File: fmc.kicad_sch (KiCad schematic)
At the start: 2 parts, among them P1 ASP-134604-01, P2 ASP-134604-01

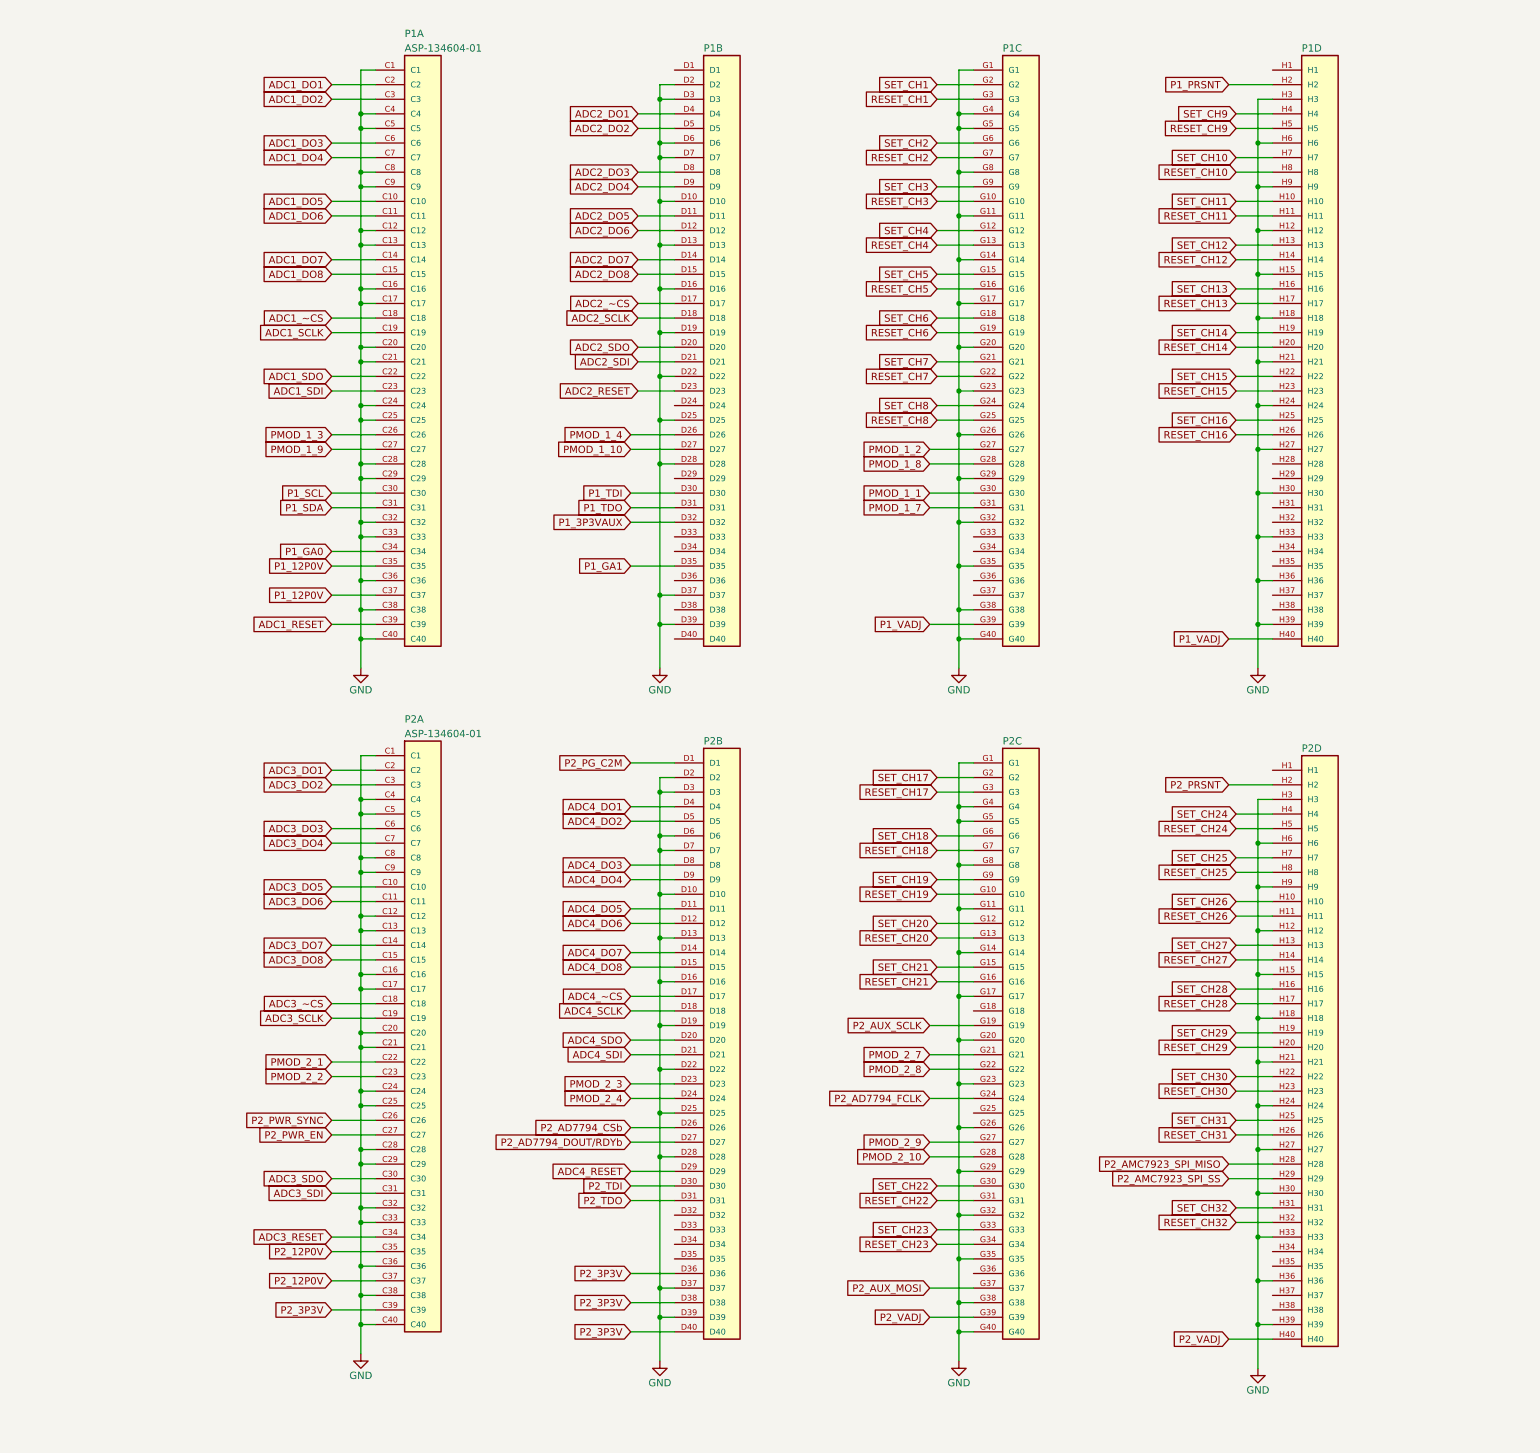
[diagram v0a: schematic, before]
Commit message: Updated Schmatics
Some outdated schematics were in the init commit. Uploded proper revision with tweaks.
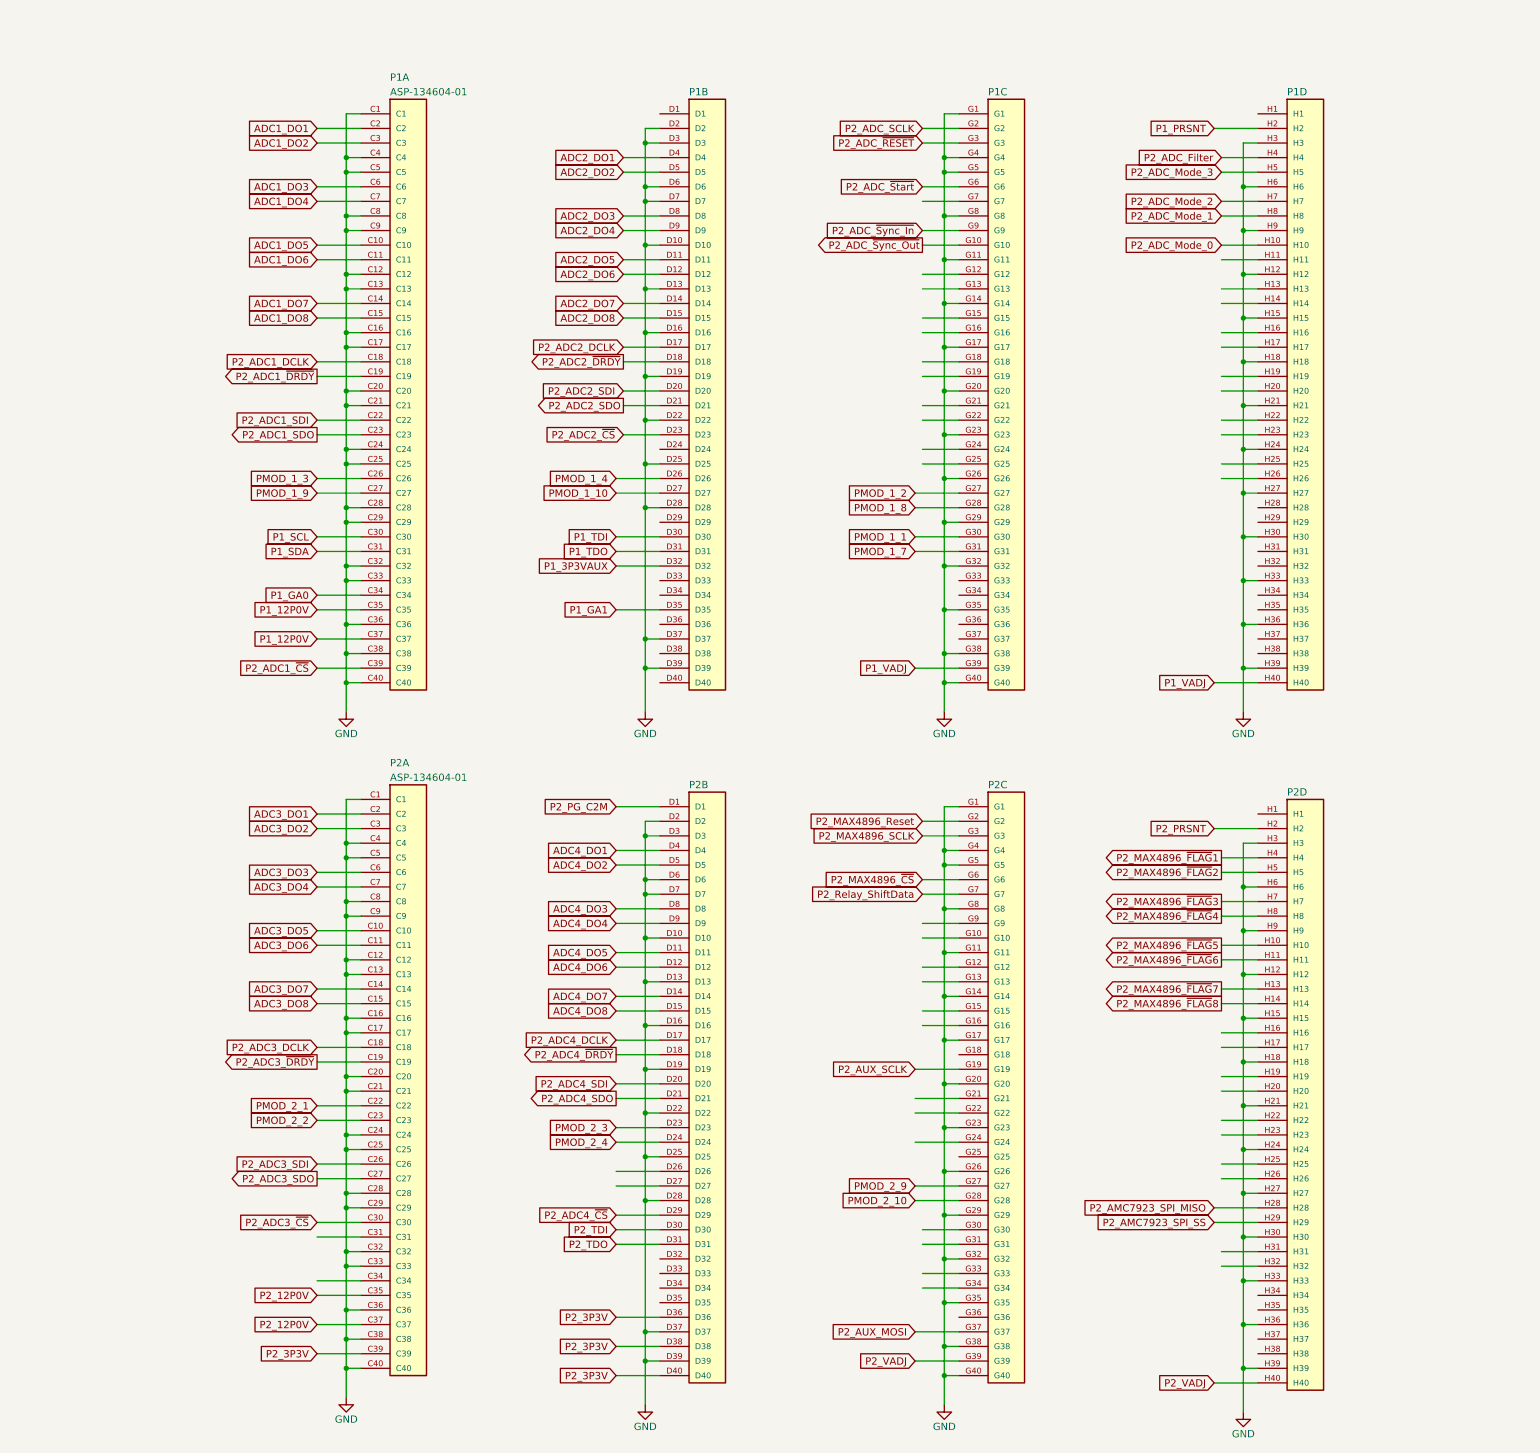
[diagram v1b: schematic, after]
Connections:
- net ADC1_RESET renamed P2_ADC1_~{CS}
- net ADC1_SCLK renamed P2_ADC1_~{DRDY}
- net ADC1_SDI renamed P2_ADC1_SDO
- net ADC1_SDO renamed P2_ADC1_SDI
- net ADC1_~CS renamed P2_ADC1_DCLK
- net ADC2_RESET renamed P2_ADC2_~{CS}
- net ADC2_SCLK renamed P2_ADC2_~{DRDY}
- net ADC2_SDI renamed P2_ADC2_SDO
- net ADC2_SDO renamed P2_ADC2_SDI
- net ADC2_~CS renamed P2_ADC2_DCLK
- net ADC3_RESET: no longer names the net of P2.C34
- net ADC3_SCLK renamed P2_ADC3_~{DRDY}
- net ADC3_SDI: no longer names the net of P2.C31
- net ADC3_SDO renamed P2_ADC3_~{CS}
- net ADC3_~CS renamed P2_ADC3_DCLK
- net ADC4_RESET renamed P2_ADC4_~{CS}
- net ADC4_SCLK renamed P2_ADC4_~{DRDY}
- net ADC4_SDI renamed P2_ADC4_SDO
- net ADC4_SDO renamed P2_ADC4_SDI
- net ADC4_~CS renamed P2_ADC4_DCLK
- net P2_AD7794_CSb: no longer names the net of P2.D26
- net P2_AD7794_DOUT/RDYb: no longer names the net of P2.D27
- net P2_AD7794_FCLK: no longer names the net of P2.G24
- net P2_PWR_EN renamed P2_ADC3_SDO
- net P2_PWR_SYNC renamed P2_ADC3_SDI
- net PMOD_2_7: no longer names the net of P2.G21
- net PMOD_2_8: no longer names the net of P2.G22
- net RESET_CH1 renamed P2_ADC_~{RESET}
- net RESET_CH10 renamed P2_ADC_Mode_1
- net RESET_CH11: no longer names the net of P1.H11
- net RESET_CH12: no longer names the net of P1.H14
- net RESET_CH13: no longer names the net of P1.H17
- net RESET_CH14: no longer names the net of P1.H20
- net RESET_CH15: no longer names the net of P1.H23
- net RESET_CH16: no longer names the net of P1.H26
- net RESET_CH17 renamed P2_MAX4896_SCLK
- net RESET_CH18 renamed P2_Relay_ShiftData
- net RESET_CH19: no longer names the net of P2.G10
- net RESET_CH2: no longer names the net of P1.G7
- net RESET_CH20: no longer names the net of P2.G13
- net RESET_CH21: no longer names the net of P2.G16
- net RESET_CH22: no longer names the net of P2.G31
- net RESET_CH23: no longer names the net of P2.G34
- net RESET_CH24 renamed P2_MAX4896_~{FLAG}2
- net RESET_CH25 renamed P2_MAX4896_~{FLAG}4
- net RESET_CH26 renamed P2_MAX4896_~{FLAG}6
- net RESET_CH27 renamed P2_MAX4896_~{FLAG}8
- net RESET_CH28: no longer names the net of P2.H17
- net RESET_CH29: no longer names the net of P2.H20
- net RESET_CH3 renamed P2_ADC_~{Sync_Out}
- net RESET_CH30: no longer names the net of P2.H23
- net RESET_CH31: no longer names the net of P2.H26
- net RESET_CH32: no longer names the net of P2.H32
- net RESET_CH4: no longer names the net of P1.G13
- net RESET_CH5: no longer names the net of P1.G16
- net RESET_CH6: no longer names the net of P1.G19
- net RESET_CH7: no longer names the net of P1.G22
- net RESET_CH8: no longer names the net of P1.G25
- net RESET_CH9 renamed P2_ADC_Mode_3
- net SET_CH1 renamed P2_ADC_SCLK
- net SET_CH10 renamed P2_ADC_Mode_2
- net SET_CH11 renamed P2_ADC_Mode_0
- net SET_CH12: no longer names the net of P1.H13
- net SET_CH13: no longer names the net of P1.H16
- net SET_CH14: no longer names the net of P1.H19
- net SET_CH15: no longer names the net of P1.H22
- net SET_CH16: no longer names the net of P1.H25
- net SET_CH17 renamed P2_MAX4896_Reset
- net SET_CH18 renamed P2_MAX4896_~{CS}
- net SET_CH19: no longer names the net of P2.G9
- net SET_CH2 renamed P2_ADC_~{Start}
- net SET_CH20: no longer names the net of P2.G12
- net SET_CH21: no longer names the net of P2.G15
- net SET_CH22: no longer names the net of P2.G30
- net SET_CH23: no longer names the net of P2.G33
- net SET_CH24 renamed P2_MAX4896_~{FLAG}1
- net SET_CH25 renamed P2_MAX4896_~{FLAG}3
- net SET_CH26 renamed P2_MAX4896_~{FLAG}5
- net SET_CH27 renamed P2_MAX4896_~{FLAG}7
- net SET_CH28: no longer names the net of P2.H16
- net SET_CH29: no longer names the net of P2.H19
- net SET_CH3 renamed P2_ADC_~{Sync_In}
- net SET_CH30: no longer names the net of P2.H22
- net SET_CH31: no longer names the net of P2.H25
- net SET_CH32: no longer names the net of P2.H31
- net SET_CH4: no longer names the net of P1.G12
- net SET_CH5: no longer names the net of P1.G15
- net SET_CH6: no longer names the net of P1.G18
- net SET_CH7: no longer names the net of P1.G21
- net SET_CH8: no longer names the net of P1.G24
- net SET_CH9 renamed P2_ADC_Filter

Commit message: Fixed FMC mapping Issue
Fixed FMC pin mapping and added FMC pin mapping excel file
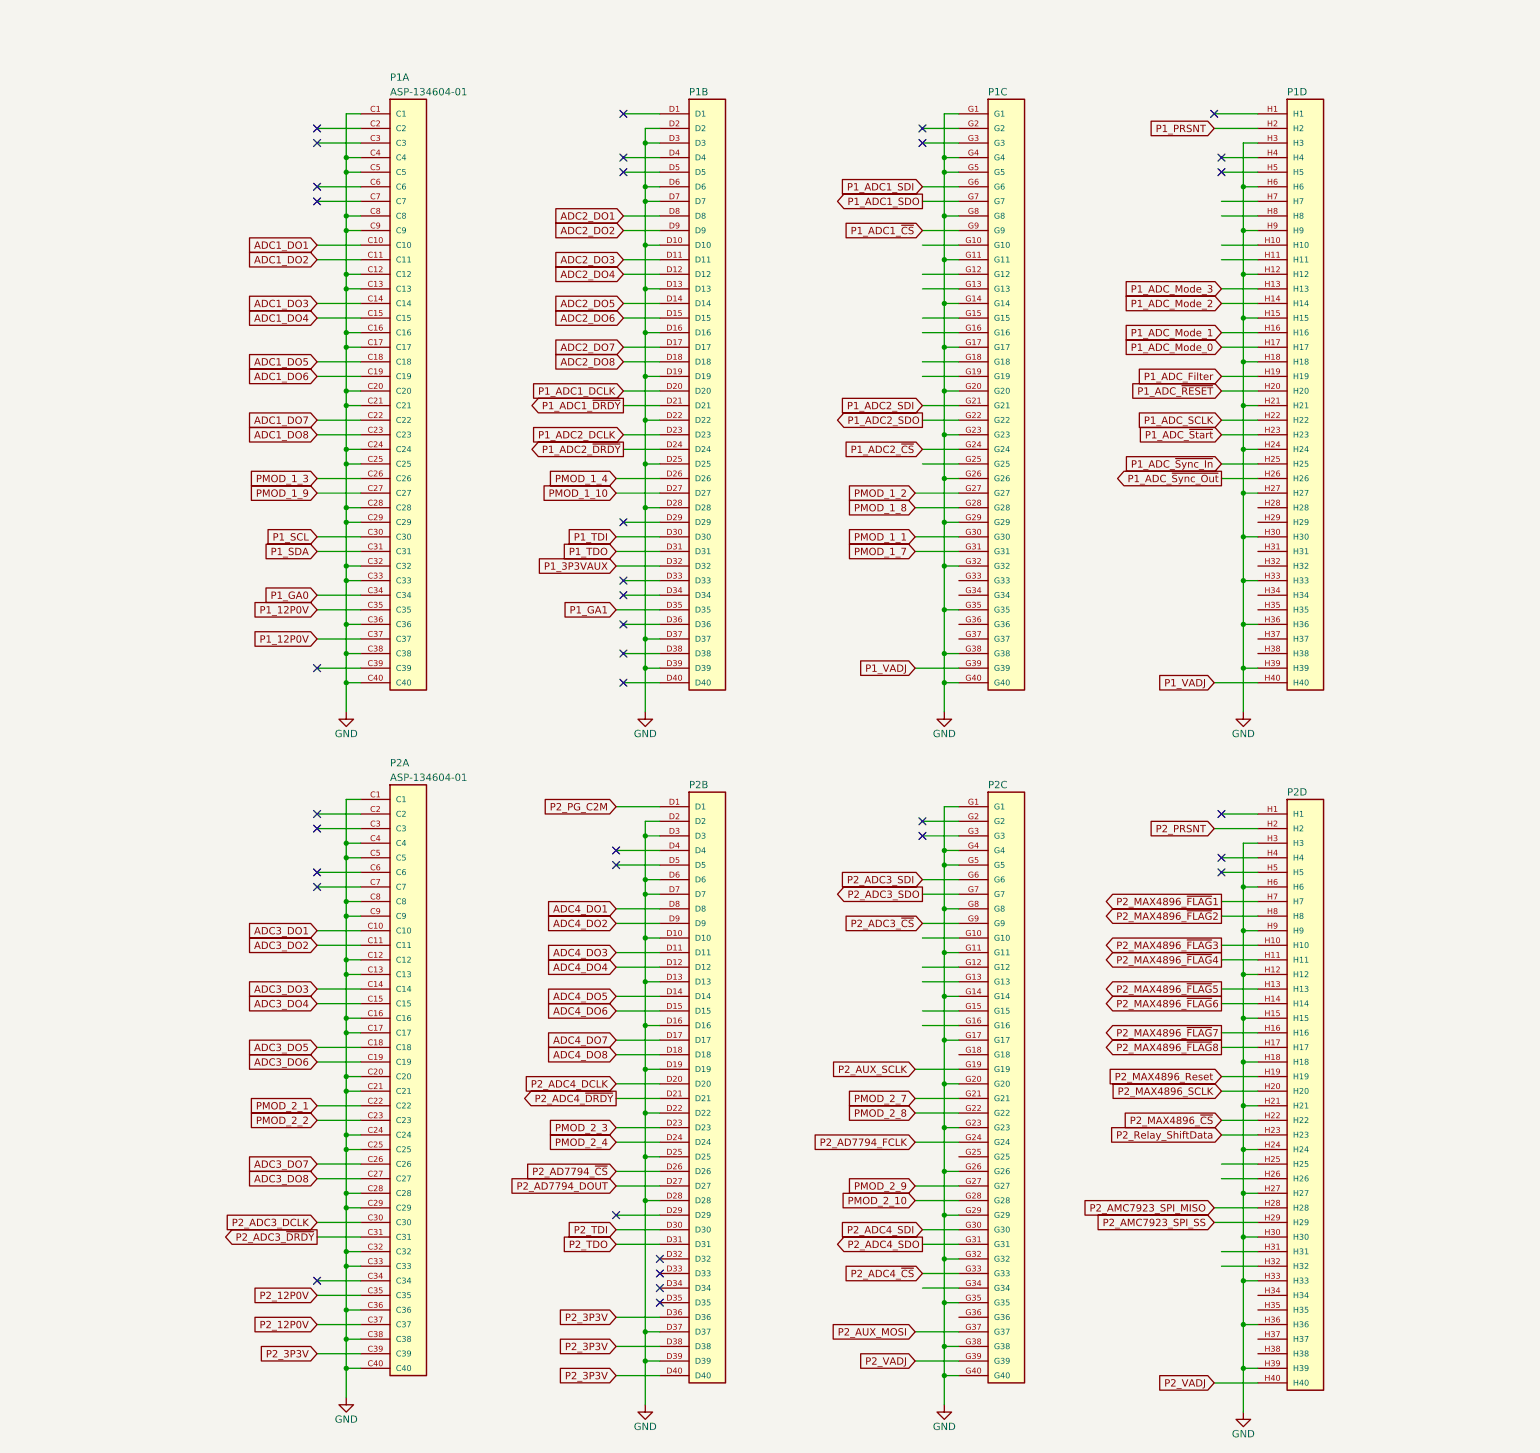
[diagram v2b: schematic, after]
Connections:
- net P2_ADC1_DCLK is gone; now on net ADC1_DO5: P1.C18
- net P2_ADC1_SDI is gone; now on net ADC1_DO7: P1.C22
- net P2_ADC1_SDO is gone; now on net ADC1_DO8: P1.C23
- net P2_ADC1_~{DRDY} is gone; now on net ADC1_DO6: P1.C19
- net P2_ADC2_DCLK is gone; now on net ADC2_DO7: P1.D17
- net P2_ADC2_~{DRDY} is gone; now on net ADC2_DO8: P1.D18
- net ADC1_DO1: now also P1.C10; no longer P1.C2
- net ADC1_DO2: now also P1.C11; no longer P1.C3
- net ADC1_DO3: now also P1.C14; no longer P1.C6
- net ADC1_DO4: now also P1.C15; no longer P1.C7
- net ADC1_DO5: no longer P1.C10
- net ADC1_DO6: no longer P1.C11
- net ADC1_DO7: no longer P1.C14
- net ADC1_DO8: no longer P1.C15
- net ADC2_DO1: now also P1.D8; no longer P1.D4
- net ADC2_DO2: now also P1.D9; no longer P1.D5
- net ADC2_DO3: now also P1.D11; no longer P1.D8
- net ADC2_DO4: now also P1.D12; no longer P1.D9
- net ADC2_DO5: now also P1.D14; no longer P1.D11
- net ADC2_DO6: now also P1.D15; no longer P1.D12
- net ADC2_DO7: no longer P1.D14
- net ADC2_DO8: no longer P1.D15
- net ADC3_DO1: now also P2.C10; no longer P2.C2
- net ADC3_DO2: now also P2.C11; no longer P2.C3
- net ADC3_DO3: now also P2.C14; no longer P2.C6
- net ADC3_DO4: now also P2.C15; no longer P2.C7
- net ADC3_DO5: now also P2.C18; no longer P2.C10
- net ADC3_DO6: now also P2.C19; no longer P2.C11
- net ADC3_DO7: now also P2.C26; no longer P2.C14
- net ADC3_DO8: now also P2.C27; no longer P2.C15
- net ADC4_DO1: now also P2.D8; no longer P2.D4
- net ADC4_DO2: now also P2.D9; no longer P2.D5
- net ADC4_DO3: now also P2.D11; no longer P2.D8
- net ADC4_DO4: now also P2.D12; no longer P2.D9
- net ADC4_DO5: now also P2.D14; no longer P2.D11
- net ADC4_DO6: now also P2.D15; no longer P2.D12
- net ADC4_DO7: now also P2.D17; no longer P2.D14
- net ADC4_DO8: now also P2.D18; no longer P2.D15
- net P2_ADC3_DCLK: now also P2.C30; no longer P2.C18
- net P2_ADC3_SDI: now also P2.G6; no longer P2.C26
- net P2_ADC3_SDO: now also P2.G7; no longer P2.C27
- net P2_ADC3_~{CS}: now also P2.G9; no longer P2.C30
- net P2_ADC3_~{DRDY}: now also P2.C31; no longer P2.C19
- net P2_ADC4_DCLK: now also P2.D20; no longer P2.D17
- net P2_ADC4_SDI: now also P2.G30; no longer P2.D20
- net P2_ADC4_SDO: now also P2.G31; no longer P2.D21
- net P2_ADC4_~{CS}: now also P2.G33; no longer P2.D29
- net P2_ADC4_~{DRDY}: now also P2.D21; no longer P2.D18
- net P2_MAX4896_Reset: now also P2.H19; no longer P2.G2
- net P2_MAX4896_SCLK: now also P2.H20; no longer P2.G3
- net P2_MAX4896_~{CS}: now also P2.H22; no longer P2.G6
- net P2_MAX4896_~{FLAG}1: now also P2.H7; no longer P2.H4
- net P2_MAX4896_~{FLAG}2: now also P2.H8; no longer P2.H5
- net P2_MAX4896_~{FLAG}3: now also P2.H10; no longer P2.H7
- net P2_MAX4896_~{FLAG}4: now also P2.H11; no longer P2.H8
- net P2_MAX4896_~{FLAG}5: now also P2.H13; no longer P2.H10
- net P2_MAX4896_~{FLAG}6: now also P2.H14; no longer P2.H11
- net P2_MAX4896_~{FLAG}7: now also P2.H16; no longer P2.H13
- net P2_MAX4896_~{FLAG}8: now also P2.H17; no longer P2.H14
- net P2_Relay_ShiftData: now also P2.H23; no longer P2.G7
- net PMOD_2_7: now reaches P2.G21
- net PMOD_2_8: now reaches P2.G22
- net P2_AD7794_FCLK: now reaches P2.G24
- net P1_ADC2_~{DRDY}: now reaches P1.D24
- net P2_AD7794_~{CS}: now reaches P2.D26
- net P2_AD7794_DOUT: now reaches P2.D27
- net P1_ADC2_SDI: now reaches P1.G21
- net P1_ADC2_SDO: now reaches P1.G22
- net P1_ADC2_~{CS}: now reaches P1.G24
- net P1_ADC1_SDO: now reaches P1.G7
- net P1_ADC_Mode_3: now reaches P1.H13
- net P1_ADC_Mode_2: now reaches P1.H14
- net P1_ADC_Mode_1: now reaches P1.H16
- net P1_ADC_Mode_0: now reaches P1.H17
- net P1_ADC_Filter: now reaches P1.H19
- net P1_ADC_~{RESET}: now reaches P1.H20
- net P1_ADC_SCLK: now reaches P1.H22
- net P1_ADC_~{Start}: now reaches P1.H23
- net P1_ADC_~{Sync_In}: now reaches P1.H25
- net P1_ADC_~{Sync_Out}: now reaches P1.H26
- net P2_ADC1_~{CS}: no longer names the net of P1.C39
- net P2_ADC2_SDI renamed P1_ADC1_DCLK
- net P2_ADC2_SDO renamed P1_ADC1_~{DRDY}
- net P2_ADC2_~{CS} renamed P1_ADC2_DCLK
- net P2_ADC_Filter: no longer names the net of P1.H4
- net P2_ADC_Mode_0: no longer names the net of P1.H10
- net P2_ADC_Mode_1: no longer names the net of P1.H8
- net P2_ADC_Mode_2: no longer names the net of P1.H7
- net P2_ADC_Mode_3: no longer names the net of P1.H5
- net P2_ADC_SCLK: no longer names the net of P1.G2
- net P2_ADC_~{RESET}: no longer names the net of P1.G3
- net P2_ADC_~{Start} renamed P1_ADC1_SDI
- net P2_ADC_~{Sync_In} renamed P1_ADC1_~{CS}
- net P2_ADC_~{Sync_Out}: no longer names the net of P1.G10
- no-connect marks 0 -> 36
